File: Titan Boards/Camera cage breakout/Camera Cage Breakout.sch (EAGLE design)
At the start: 5 parts

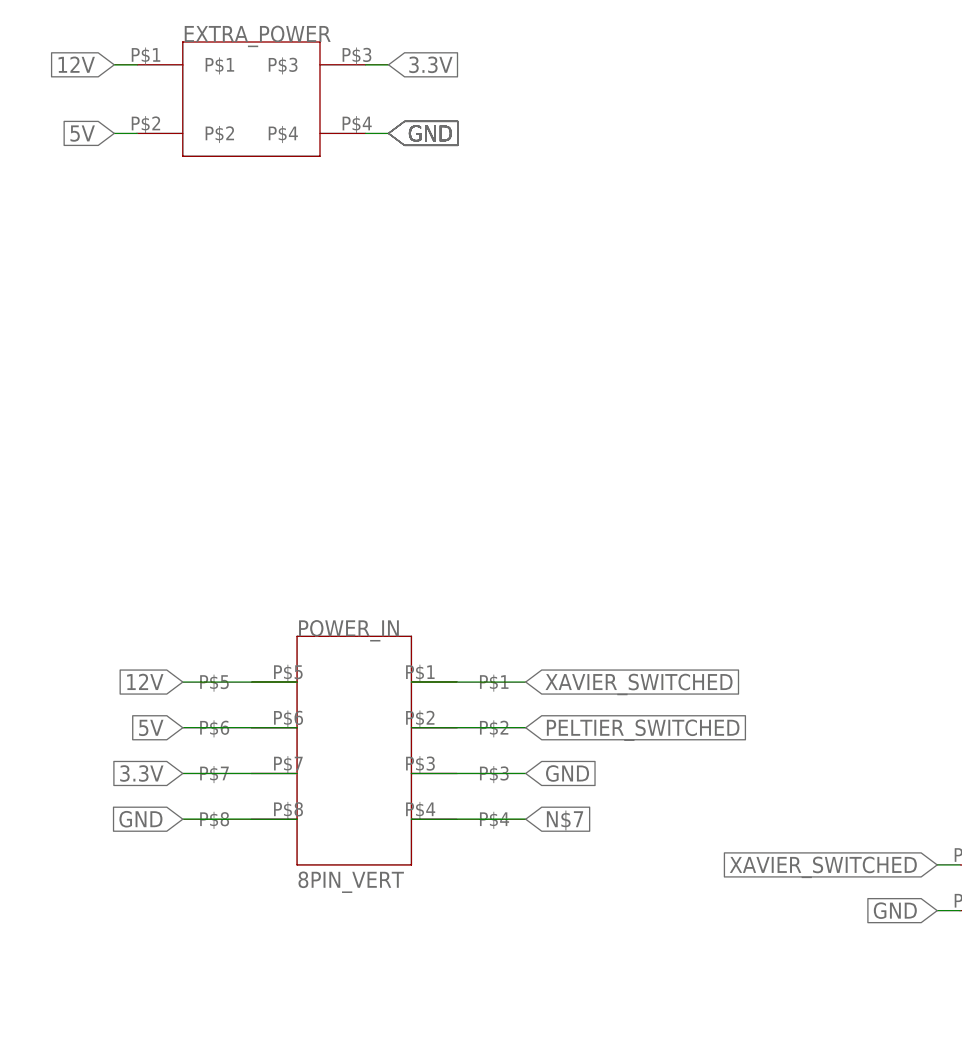
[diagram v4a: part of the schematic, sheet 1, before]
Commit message: schematic work for camera cage breakout
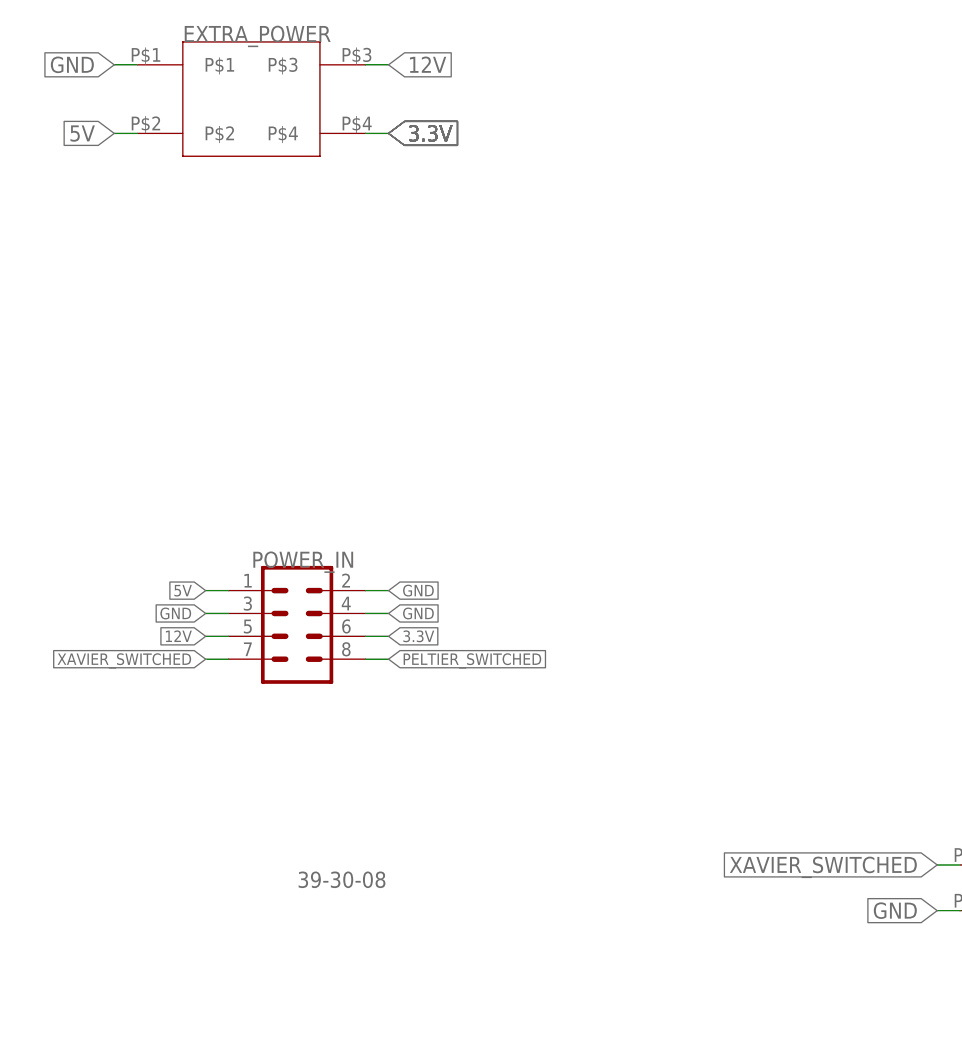
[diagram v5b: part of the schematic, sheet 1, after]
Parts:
- POWER_IN: value 8PIN_VERT -> 39-30-08; device Vertical_Connectors:8PIN_VERT -> con-molex-mini-fit:39-30-08
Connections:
- removed net N$7: POWER_IN.P$4
- net 12V: now also EXTRA_POWER.P$3, POWER_IN.5; no longer EXTRA_POWER.P$1, POWER_IN.P$5
- net 3.3V: now also EXTRA_POWER.P$4, POWER_IN.6; no longer EXTRA_POWER.P$3, POWER_IN.P$7
- net 5V: now also POWER_IN.1; no longer POWER_IN.P$6
- net GND: now also EXTRA_POWER.P$1, POWER_IN.2, POWER_IN.3, POWER_IN.4; no longer EXTRA_POWER.P$4, POWER_IN.P$3, POWER_IN.P$8
- net PELTIER_SWITCHED: now also POWER_IN.8; no longer POWER_IN.P$2
- net XAVIER_SWITCHED: now also POWER_IN.7; no longer POWER_IN.P$1
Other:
- moved on the sheet: POWER_IN
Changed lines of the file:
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@@
 <part name="FRAME1" library="frames" library_urn="urn:adsk.eagle:library:229" deviceset="A3L-LOC" device="" value="a"/>
 <part name="FRAME2" library="frames" library_urn="urn:adsk.eagle:library:229" deviceset="A3L-LOC" device="" value="a"/>
-<part name="POWER_IN" library="Vertical_Connectors" deviceset="8PIN_VERT" device=""/>
+<part name="POWER_IN" library="con-molex-mini-fit" deviceset="39-30-?08?" device=""/>
 <part name="XAVIER" library="Vertical_Connectors" deviceset="2PIN-VERT" device=""/>
 <part name="MYNT_CAMERA_NETWORK_SWITCH" library="Vertical_Connectors" deviceset="4PIN-VERT" device=""/>
@@
 </instance>
 <instance part="POWER_IN" gate="G$1" x="38.1" y="83.82" smashed="yes">
-<attribute name="NAME" x="38.1" y="83.82" size="1.778" layer="95"/>
+<attribute name="NAME" x="33.02" y="91.44" size="1.778" layer="95"/>
 <attribute name="VALUE" x="38.1" y="55.88" size="1.778" layer="96"/>
 </instance>
@@
 </segment>
 <segment>
-<pinref part="POWER_IN" gate="G$1" pin="P$8"/>
-<wire x1="38.1" y1="63.5" x2="25.4" y2="63.5" width="0.1524" layer="91"/>
-<label x="25.4" y="63.5" size="1.778" layer="95" rot="R180" xref="yes"/>
+<pinref part="POWER_IN" gate="G$1" pin="4"/>
+<wire x1="45.72" y1="86.36" x2="48.26" y2="86.36" width="0.1524" layer="91"/>
+<label x="48.26" y="86.36" size="1.27" layer="95" xref="yes"/>
 </segment>
 <segment>
-<pinref part="EXTRA_POWER" gate="G$1" pin="P$4"/>
-<wire x1="45.72" y1="139.7" x2="48.26" y2="139.7" width="0.1524" layer="91"/>
-<label x="48.26" y="139.7" size="1.778" layer="95" xref="yes"/>
-<label x="48.26" y="139.7" size="1.778" layer="95" xref="yes"/>
-<label x="48.26" y="139.7" size="1.778" layer="95" xref="yes"/>
-<label x="48.26" y="139.7" size="1.778" layer="95" xref="yes"/>
+<pinref part="POWER_IN" gate="G$1" pin="2"/>
+<wire x1="45.72" y1="88.9" x2="48.26" y2="88.9" width="0.1524" layer="91"/>
+<label x="48.26" y="88.9" size="1.27" layer="95" xref="yes"/>
 </segment>
 <segment>
-<pinref part="POWER_IN" gate="G$1" pin="P$3"/>
-<wire x1="50.8" y1="68.58" x2="63.5" y2="68.58" width="0.1524" layer="91"/>
-<label x="63.5" y="68.58" size="1.778" layer="95" xref="yes"/>
+<pinref part="EXTRA_POWER" gate="G$1" pin="P$1"/>
+<wire x1="20.32" y1="147.32" x2="17.78" y2="147.32" width="0.1524" layer="91"/>
+<label x="17.78" y="147.32" size="1.778" layer="95" rot="R180" xref="yes"/>
+</segment>
+<segment>
+<pinref part="POWER_IN" gate="G$1" pin="3"/>
+<wire x1="30.48" y1="86.36" x2="27.94" y2="86.36" width="0.1524" layer="91"/>
+<label x="27.94" y="86.36" size="1.27" layer="95" rot="R180" xref="yes"/>
 </segment>
 </net>
@@
 </segment>
 <segment>
-<pinref part="POWER_IN" gate="G$1" pin="P$6"/>
-<wire x1="38.1" y1="73.66" x2="25.4" y2="73.66" width="0.1524" layer="91"/>
-<label x="25.4" y="73.66" size="1.778" layer="95" rot="R180" xref="yes"/>
-</segment>
-<segment>
 <pinref part="EXTRA_POWER" gate="G$1" pin="P$2"/>
 <wire x1="20.32" y1="139.7" x2="17.78" y2="139.7" width="0.1524" layer="91"/>
 <label x="17.78" y="139.7" size="1.778" layer="95" rot="R180" xref="yes"/>
+</segment>
+<segment>
+<pinref part="POWER_IN" gate="G$1" pin="1"/>
+<wire x1="30.48" y1="88.9" x2="27.94" y2="88.9" width="0.1524" layer="91"/>
+<label x="27.94" y="88.9" size="1.27" layer="95" rot="R180" xref="yes"/>
 </segment>
 </net>
@@
 </segment>
 <segment>
-<pinref part="POWER_IN" gate="G$1" pin="P$2"/>
-<wire x1="50.8" y1="73.66" x2="63.5" y2="73.66" width="0.1524" layer="91"/>
-<label x="63.5" y="73.66" size="1.778" layer="95" xref="yes"/>
+<pinref part="POWER_IN" gate="G$1" pin="8"/>
+<wire x1="45.72" y1="81.28" x2="48.26" y2="81.28" width="0.1524" layer="91"/>
+<label x="48.26" y="81.28" size="1.27" layer="95" xref="yes"/>
 </segment>
 </net>
@@
 </segment>
 <segment>
-<pinref part="POWER_IN" gate="G$1" pin="P$1"/>
-<wire x1="50.8" y1="78.74" x2="63.5" y2="78.74" width="0.1524" layer="91"/>
-<label x="63.5" y="78.74" size="1.778" layer="95" xref="yes"/>
+<pinref part="POWER_IN" gate="G$1" pin="7"/>
+<wire x1="30.48" y1="81.28" x2="27.94" y2="81.28" width="0.1524" layer="91"/>
+<label x="27.94" y="81.28" size="1.27" layer="95" rot="R180" xref="yes"/>
 </segment>
 </net>
 <net name="12V" class="0">
-<segment>
-<pinref part="POWER_IN" gate="G$1" pin="P$5"/>
-<wire x1="38.1" y1="78.74" x2="25.4" y2="78.74" width="0.1524" layer="91"/>
-<label x="25.4" y="78.74" size="1.778" layer="95" rot="R180" xref="yes"/>
-</segment>
-<segment>
-<pinref part="EXTRA_POWER" gate="G$1" pin="P$1"/>
-<wire x1="20.32" y1="147.32" x2="17.78" y2="147.32" width="0.1524" layer="91"/>
-<label x="17.78" y="147.32" size="1.778" layer="95" rot="R180" xref="yes"/>
-</segment>
-</net>
-<net name="3.3V" class="0">
-<segment>
-<pinref part="POWER_IN" gate="G$1" pin="P$7"/>
-<wire x1="38.1" y1="68.58" x2="25.4" y2="68.58" width="0.1524" layer="91"/>
-<label x="25.4" y="68.58" size="1.778" layer="95" rot="R180" xref="yes"/>
-</segment>
 <segment>
 <pinref part="EXTRA_POWER" gate="G$1" pin="P$3"/>
@@
 <label x="48.26" y="147.32" size="1.778" layer="95" xref="yes"/>
 </segment>
-</net>
-<net name="N$7" class="0">
 <segment>
-<pinref part="POWER_IN" gate="G$1" pin="P$4"/>
-<wire x1="50.8" y1="63.5" x2="63.5" y2="63.5" width="0.1524" layer="91"/>
-<label x="63.5" y="63.5" size="1.778" layer="95" xref="yes"/>
+<pinref part="POWER_IN" gate="G$1" pin="5"/>
+<wire x1="30.48" y1="83.82" x2="27.94" y2="83.82" width="0.1524" layer="91"/>
+<label x="27.94" y="83.82" size="1.27" layer="95" rot="R180" xref="yes"/>
 </segment>
 </net>
+<net name="3.3V" class="0">
+<segment>
+<pinref part="EXTRA_POWER" gate="G$1" pin="P$4"/>
+<wire x1="45.72" y1="139.7" x2="48.26" y2="139.7" width="0.1524" layer="91"/>
+<label x="48.26" y="139.7" size="1.778" layer="95" xref="yes"/>
+<label x="48.26" y="139.7" size="1.778" layer="95" xref="yes"/>
+<label x="48.26" y="139.7" size="1.778" layer="95" xref="yes"/>
+<label x="48.26" y="139.7" size="1.778" layer="95" xref="yes"/>
+</segment>
+<segment>
+<pinref part="POWER_IN" gate="G$1" pin="6"/>
+<wire x1="45.72" y1="83.82" x2="48.26" y2="83.82" width="0.1524" layer="91"/>
+<label x="48.26" y="83.82" size="1.27" layer="95" xref="yes"/>
+</segment>
+</net>

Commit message: final camera cage breakout with gerbers
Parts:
- added U$1: CAMERA_CAGE_TEST, 3M_929852_Connector:CAMERA_CAGE_TEST
- renumbered MYNT_CAMERA_NETWORK_SWITCH to MYNT_CAMERA, PELTIER_AND_FANS to PLTA_FANS
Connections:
- net 12V: now also U$1.12V
- net 3.3V: now also U$1.GND
- net 5V: now also U$1.5V
- net GND: now also U$1.3.3V
- net PELTIER_SWITCHED: now also U$1.XAVIER_SWITCHED
- net XAVIER_SWITCHED: now also U$1.PELTIER_SWITCHED
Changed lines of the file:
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@@
 <part name="POWER_IN" library="con-molex-mini-fit" deviceset="39-30-?08?" device=""/>
 <part name="XAVIER" library="Vertical_Connectors" deviceset="2PIN-VERT" device=""/>
-<part name="MYNT_CAMERA_NETWORK_SWITCH" library="Vertical_Connectors" deviceset="4PIN-VERT" device=""/>
-<part name="PELTIER_AND_FANS" library="Vertical_Connectors" deviceset="4PIN-VERT" device=""/>
+<part name="MYNT_CAMERA" library="Vertical_Connectors" deviceset="4PIN-VERT" device=""/>
+<part name="PLTA_FANS" library="Vertical_Connectors" deviceset="4PIN-VERT" device=""/>
 <part name="EXTRA_POWER" library="Vertical_Connectors" deviceset="4PIN-VERT" device=""/>
+<part name="U$1" library="3M_929852_Connector" deviceset="CAMERA_CAGE_TEST" device=""/>
 </parts>
 <sheets>
@@
 <attribute name="NAME" x="116.84" y="60.96" size="1.778" layer="95"/>
 </instance>
-<instance part="MYNT_CAMERA_NETWORK_SWITCH" gate="G$1" x="177.8" y="101.6" smashed="yes">
+<instance part="MYNT_CAMERA" gate="G$1" x="177.8" y="101.6" smashed="yes">
 <attribute name="NAME" x="175.26" y="111.76" size="1.778" layer="95"/>
 </instance>
-<instance part="PELTIER_AND_FANS" gate="G$1" x="177.8" y="81.28" smashed="yes">
+<instance part="PLTA_FANS" gate="G$1" x="177.8" y="81.28" smashed="yes">
 <attribute name="NAME" x="175.26" y="91.44" size="1.778" layer="95"/>
 </instance>
 <instance part="EXTRA_POWER" gate="G$1" x="27.94" y="139.7" smashed="yes">
 <attribute name="NAME" x="25.4" y="149.86" size="1.778" layer="95"/>
+</instance>
+<instance part="U$1" gate="G$1" x="243.84" y="114.3" smashed="yes">
+<attribute name="NAME" x="248.92" y="114.3" size="1.778" layer="95"/>
 </instance>
 </instances>
@@
 <net name="GND" class="0">
 <segment>
-<pinref part="MYNT_CAMERA_NETWORK_SWITCH" gate="G$1" pin="P$3"/>
-<pinref part="MYNT_CAMERA_NETWORK_SWITCH" gate="G$1" pin="P$4"/>
+<pinref part="MYNT_CAMERA" gate="G$1" pin="P$3"/>
+<pinref part="MYNT_CAMERA" gate="G$1" pin="P$4"/>
 <wire x1="195.58" y1="109.22" x2="195.58" y2="106.68" width="0.1524" layer="91"/>
 <wire x1="195.58" y1="106.68" x2="195.58" y2="101.6" width="0.1524" layer="91"/>
@@
 </segment>
 <segment>
-<pinref part="PELTIER_AND_FANS" gate="G$1" pin="P$3"/>
-<pinref part="PELTIER_AND_FANS" gate="G$1" pin="P$4"/>
+<pinref part="PLTA_FANS" gate="G$1" pin="P$3"/>
+<pinref part="PLTA_FANS" gate="G$1" pin="P$4"/>
 <wire x1="195.58" y1="88.9" x2="195.58" y2="86.36" width="0.1524" layer="91"/>
 <wire x1="195.58" y1="86.36" x2="195.58" y2="81.28" width="0.1524" layer="91"/>
@@
 <label x="27.94" y="86.36" size="1.27" layer="95" rot="R180" xref="yes"/>
 </segment>
+<segment>
+<pinref part="U$1" gate="G$1" pin="3.3V"/>
+<wire x1="238.76" y1="101.6" x2="236.22" y2="101.6" width="0.1524" layer="91"/>
+<label x="231.14" y="101.6" size="1.778" layer="95"/>
+</segment>
 </net>
 <net name="5V" class="0">
 <segment>
-<pinref part="MYNT_CAMERA_NETWORK_SWITCH" gate="G$1" pin="P$1"/>
-<pinref part="MYNT_CAMERA_NETWORK_SWITCH" gate="G$1" pin="P$2"/>
+<pinref part="MYNT_CAMERA" gate="G$1" pin="P$1"/>
+<pinref part="MYNT_CAMERA" gate="G$1" pin="P$2"/>
 <wire x1="170.18" y1="109.22" x2="170.18" y2="106.68" width="0.1524" layer="91"/>
 <wire x1="170.18" y1="106.68" x2="170.18" y2="101.6" width="0.1524" layer="91"/>
@@
 <label x="27.94" y="88.9" size="1.27" layer="95" rot="R180" xref="yes"/>
 </segment>
+<segment>
+<pinref part="U$1" gate="G$1" pin="5V"/>
+<wire x1="238.76" y1="106.68" x2="236.22" y2="106.68" width="0.1524" layer="91"/>
+<label x="231.14" y="106.68" size="1.778" layer="95"/>
+</segment>
 </net>
 <net name="PELTIER_SWITCHED" class="0">
 <segment>
-<pinref part="PELTIER_AND_FANS" gate="G$1" pin="P$1"/>
-<pinref part="PELTIER_AND_FANS" gate="G$1" pin="P$2"/>
+<pinref part="PLTA_FANS" gate="G$1" pin="P$1"/>
+<pinref part="PLTA_FANS" gate="G$1" pin="P$2"/>
 <wire x1="170.18" y1="88.9" x2="170.18" y2="86.36" width="0.1524" layer="91"/>
 <wire x1="170.18" y1="86.36" x2="170.18" y2="81.28" width="0.1524" layer="91"/>
@@
 <wire x1="45.72" y1="81.28" x2="48.26" y2="81.28" width="0.1524" layer="91"/>
 <label x="48.26" y="81.28" size="1.27" layer="95" xref="yes"/>
+</segment>
+<segment>
+<pinref part="U$1" gate="G$1" pin="XAVIER_SWITCHED"/>
+<wire x1="238.76" y1="91.44" x2="236.22" y2="91.44" width="0.1524" layer="91"/>
+<label x="213.36" y="91.44" size="1.778" layer="95"/>
 </segment>
 </net>
@@
 <label x="27.94" y="81.28" size="1.27" layer="95" rot="R180" xref="yes"/>
 </segment>
+<segment>
+<pinref part="U$1" gate="G$1" pin="PELTIER_SWITCHED"/>
+<wire x1="238.76" y1="96.52" x2="236.22" y2="96.52" width="0.1524" layer="91"/>
+<label x="213.36" y="96.52" size="1.778" layer="95"/>
+</segment>
 </net>
 <net name="12V" class="0">
@@
 <wire x1="30.48" y1="83.82" x2="27.94" y2="83.82" width="0.1524" layer="91"/>
 <label x="27.94" y="83.82" size="1.27" layer="95" rot="R180" xref="yes"/>
+</segment>
+<segment>
+<pinref part="U$1" gate="G$1" pin="12V"/>
+<wire x1="238.76" y1="111.76" x2="236.22" y2="111.76" width="0.1524" layer="91"/>
+<label x="231.14" y="111.76" size="1.778" layer="95"/>
 </segment>
 </net>
@@
 <label x="48.26" y="83.82" size="1.27" layer="95" xref="yes"/>
 </segment>
+<segment>
+<pinref part="U$1" gate="G$1" pin="GND"/>
+<wire x1="238.76" y1="86.36" x2="236.22" y2="86.36" width="0.1524" layer="91"/>
+<label x="231.14" y="86.36" size="1.778" layer="95"/>
+</segment>
 </net>
